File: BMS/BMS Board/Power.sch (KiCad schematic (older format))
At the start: 16 parts, among them K1 G5PZ-1A_DC12, M21 AO3402, P1 Power_Pad, P2 Power_Pad, P3 Power_Pad, P4 Power_Pad, P5 Power_Pad, P6 Power_Pad, Q1 STD12N60DM2AG

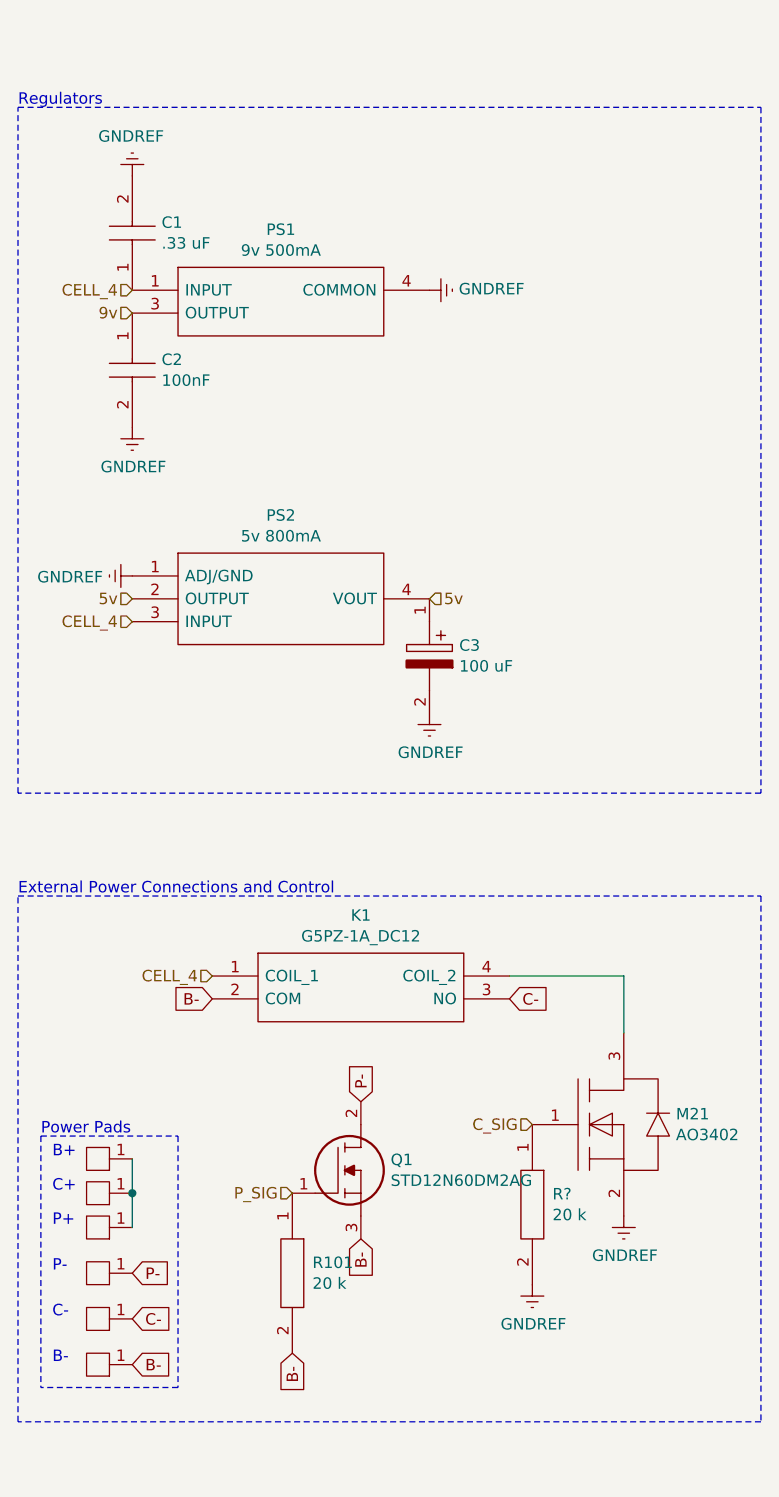
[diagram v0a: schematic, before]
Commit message: changed ui components to be classes instead of methods in Screen class
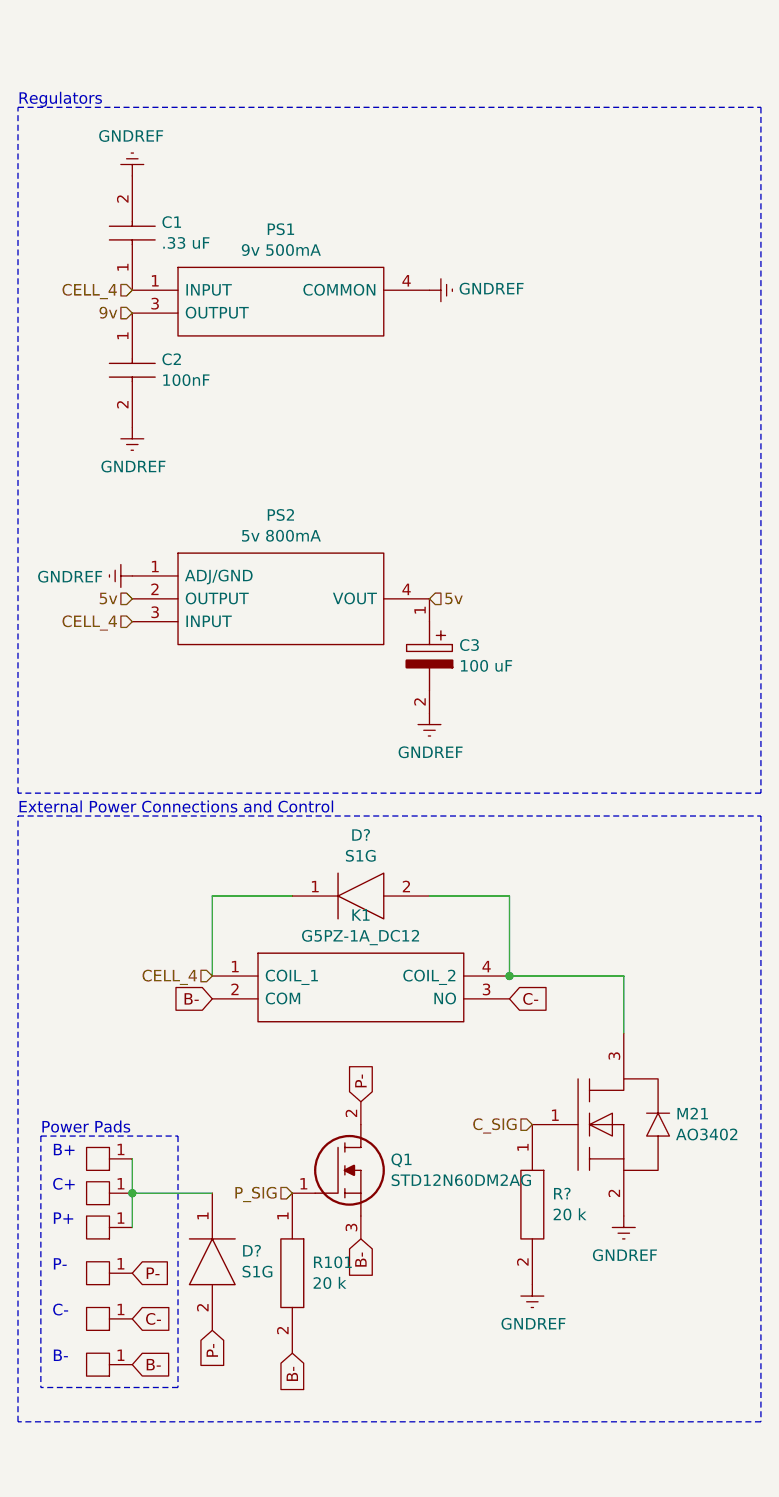
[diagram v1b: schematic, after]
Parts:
- added D? (x2): S1G, DIOM5227X250N, symbol SamacSys_Parts:S1G
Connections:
- net CELL_4: now also D?.1
- net P-: now also D?.2
- net at P1.1, P2.1, P3.1: now also D?.1
- net at K1.4 (COIL_2), M21.3 (D): now also D?.2
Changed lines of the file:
@@
 Text GLabel 3050 8350 2    50   Input ~ 0
 C-
-Wire Wire Line
-	3050 7650 3050 7800
 Connection ~ 3050 7800
 Wire Wire Line
@@
 Power Pads
 Wire Notes Line
-	2550 8800 2550 6500
-Wire Notes Line
-	2550 6500 5800 6500
-Wire Notes Line
-	5800 6500 5800 8800
+	2550 6150 5800 6150
 Wire Notes Line
 	5800 8800 2550 8800
-Text Notes 2550 6500 0    50   ~ 0
+Text Notes 2550 6150 0    50   ~ 0
 External Power Connections and Control
 Wire Notes Line
@@
 Text GLabel 3750 8500 3    50   Input ~ 0
 B-
+$Comp
+L SamacSys_Parts:S1G D?
+U 1 1 5EF4840C
+P 4050 6500
+F 0 "D?" H 4050 6765 50  0000 C CNN
+F 1 "S1G" H 4050 6674 50  0000 C CNN
+F 2 "DIOM5227X250N" H 3750 6150 50  0001 L CNN
+F 3 "https://www.onsemi.com/pub/Collateral/S1M-D.pdf" H 3750 6050 50  0001 L CNN
+F 4 "ON Semi 400V 1A, Diode, 2-Pin DO-214AC S1G" H 3750 5950 50  0001 L CNN "Description"
+F 5 "2.5" H 3750 5850 50  0001 L CNN "Height"
+F 6 "512-S1G" H 3750 5750 50  0001 L CNN "Mouser Part Number"
+F 7 "https://www.mouser.co.uk/ProductDetail/ON-Semiconductor-Fairchild/S1G?qs=RJwZ8kJo1mjiLbqXClupXw%3D%3D" H 3750 5650 50  0001 L CNN "Mouser Price/Stock"
+F 8 "ON Semiconductor" H 3750 5550 50  0001 L CNN "Manufacturer_Name"
+F 9 "S1G" H 3750 5450 50  0001 L CNN "Manufacturer_Part_Number"
+	1    4050 6500
+	1    0    0    -1
+$EndComp
+Wire Notes Line
+	2550 8800 2550 6150
+Wire Notes Line
+	5800 6150 5800 8800
+Wire Wire Line
+	3750 6500 3400 6500
+Wire Wire Line
+	3400 6500 3400 6850
+Wire Wire Line
+	4350 6500 4700 6500
+Wire Wire Line
+	4700 6500 4700 6850
+Connection ~ 4700 6850
+$Comp
+L SamacSys_Parts:S1G D?
+U 1 1 5EF4C90F
+P 3400 8100
+F 0 "D?" V 3354 8228 50  0000 L CNN
+F 1 "S1G" V 3445 8228 50  0000 L CNN
+F 2 "DIOM5227X250N" H 3100 7750 50  0001 L CNN
+F 3 "https://www.onsemi.com/pub/Collateral/S1M-D.pdf" H 3100 7650 50  0001 L CNN
+F 4 "ON Semi 400V 1A, Diode, 2-Pin DO-214AC S1G" H 3100 7550 50  0001 L CNN "Description"
+F 5 "2.5" H 3100 7450 50  0001 L CNN "Height"
+F 6 "512-S1G" H 3100 7350 50  0001 L CNN "Mouser Part Number"
+F 7 "https://www.mouser.co.uk/ProductDetail/ON-Semiconductor-Fairchild/S1G?qs=RJwZ8kJo1mjiLbqXClupXw%3D%3D" H 3100 7250 50  0001 L CNN "Mouser Price/Stock"
+F 8 "ON Semiconductor" H 3100 7150 50  0001 L CNN "Manufacturer_Name"
+F 9 "S1G" H 3100 7050 50  0001 L CNN "Manufacturer_Part_Number"
+	1    3400 8100
+	0    1    1    0
+$EndComp
+Wire Wire Line
+	3050 7650 3050 7800
+Wire Wire Line
+	3400 7800 3050 7800
+Text GLabel 3400 8400 3    50   Input ~ 0
+P-
 $EndSCHEMATC

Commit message: "SingleDigitNumberSelector" now blinks when idle.
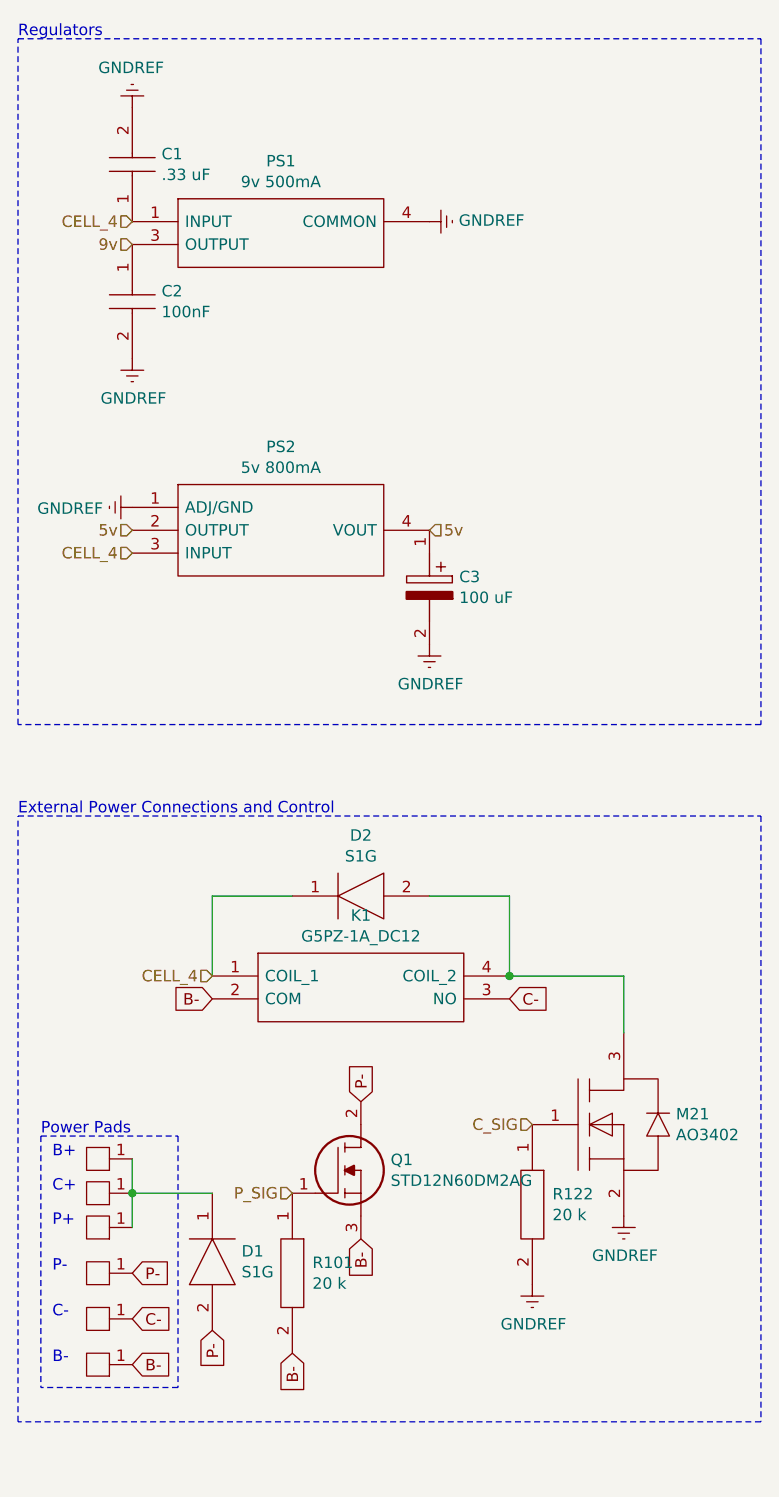
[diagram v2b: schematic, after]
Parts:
- gave numbers to parts that had none: 3
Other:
- moved on the sheet: C1, C2, C3, PS1, PS2

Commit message: ...
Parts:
- added LED3: HSMG-C170, LEDC2012X80N, symbol SamacSys_Parts:HSMG-C170
- added R143: ERJ-P06F2200V, RESC2012X70N, symbol SamacSys_Parts:ERJ-P06F2200V
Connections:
- net C_SIG: now also R143.1
- net GNDREF: now also LED3.1 (K)
- new net: LED3.2 (A), R143.2
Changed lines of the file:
@@
 P 4000 7700
 F 0 "Q1" H 4180 7746 50  0000 L CNN
-F 1 "STD12N60DM2AG" H 4180 7655 50  0000 L CNN
+F 1 "STD12N60DM2AG" H 4180 7655 50  0001 L CNN
 F 2 "STD13N60DM2" H 3750 7050 50  0001 L CNN
 F 3 "https://www.st.com/resource/en/datasheet/std12n60dm2ag.pdf" H 3750 6950 50  0001 L CNN
@@
 	-1   0    0    1
 $EndComp
-Text HLabel 4800 7500 0    50   Input ~ 0
+Text HLabel 4500 7500 0    50   Input ~ 0
 C_SIG
 Text HLabel 3750 7800 0    50   Input ~ 0
@@
 	2550 6150 5800 6150
 Wire Notes Line
-	5800 8800 2550 8800
+	5800 9050 2550 9050
 Text Notes 2550 6150 0    50   ~ 0
 External Power Connections and Control
@@
 	1    0    0    -1
 $EndComp
-Wire Notes Line
-	2550 8800 2550 6150
-Wire Notes Line
-	5800 6150 5800 8800
 Wire Wire Line
 	3750 6500 3400 6500
@@
 Text GLabel 3400 8400 3    50   Input ~ 0
 P-
+$Comp
+L SamacSys_Parts:ERJ-P06F2200V R143
+U 1 1 5EF455EC
+P 4500 7850
+F 0 "R143" V 4454 7938 50  0000 L CNN
+F 1 "ERJ-P06F2200V" H 4350 7600 50  0001 L CNN
+F 2 "RESC2012X70N" H 4350 7500 50  0001 L CNN
+F 3 "https://componentsearchengine.com/Datasheets/1/ERJ-P06F2200V.pdf" H 4700 7800 50  0001 L CNN
+F 4 "Thick Film Resistors - SMD 0805 220ohms 0.5W 1% AEC-Q200" H 4350 7400 50  0001 L CNN "Description"
+F 5 "0.7" H 4350 7300 50  0001 L CNN "Height"
+F 6 "667-ERJ-P06F2200V" H 4350 7200 50  0001 L CNN "Mouser Part Number"
+F 7 "https://www.mouser.com/Search/Refine.aspx?Keyword=667-ERJ-P06F2200V" H 4350 7100 50  0001 L CNN "Mouser Price/Stock"
+F 8 "Panasonic" H 4350 7000 50  0001 L CNN "Manufacturer_Name"
+F 9 "ERJ-P06F2200V" H 4350 6900 50  0001 L CNN "Manufacturer_Part_Number"
+F 10 "220" V 4545 7938 50  0000 L CNN "Resistance"
+	1    4500 7850
+	0    1    1    0
+$EndComp
+$Comp
+L SamacSys_Parts:HSMG-C170 LED3
+U 1 1 5EF477B4
+P 4500 8450
+F 0 "LED3" V 4496 8322 50  0000 R CNN
+F 1 "HSMG-C170" V 4405 8322 50  0000 R CNN
+F 2 "LEDC2012X80N" H 4250 8050 50  0001 L BNN
+F 3 "" H 4650 8500 50  0001 L BNN
+F 4 "Green LED, 15 mcd 170 , 2-pin 0805 SMD Package" H 4250 7950 50  0001 L BNN "Description"
+F 5 "0.8" H 4250 7850 50  0001 L BNN "Height"
+F 6 "630-HSMG-C170" H 4250 7750 50  0001 L BNN "Mouser Part Number"
+F 7 "https://www.mouser.co.uk/ProductDetail/Broadcom-Avago/HSMG-C170?qs=YDL0qNrpDT4lm8ArMPkMEA%3D%3D" H 4250 7650 50  0001 L BNN "Mouser Price/Stock"
+F 8 "Avago Technologies" H 4250 7550 50  0001 L BNN "Manufacturer_Name"
+F 9 "HSMG-C170" H 4250 7450 50  0001 L BNN "Manufacturer_Part_Number"
+	1    4500 8450
+	0    -1   -1   0
+$EndComp
+$Comp
+L power:GNDREF #PWR0155
+U 1 1 5EF48294
+P 4500 8800
+F 0 "#PWR0155" H 4500 8550 50  0001 C CNN
+F 1 "GNDREF" H 4505 8627 50  0000 C CNN
+F 2 "" H 4500 8800 50  0001 C CNN
+F 3 "" H 4500 8800 50  0001 C CNN
+	1    4500 8800
+	1    0    0    -1
+$EndComp
+Wire Notes Line
+	2550 9050 2550 6150
+Wire Notes Line
+	5800 6150 5800 9050
+Wire Wire Line
+	4500 7500 4800 7500
+Connection ~ 4800 7500
 $EndSCHEMATC

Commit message: workin on BMS also reset my computer so KiCad added some recovery files
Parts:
- M21: symbol MOSFET:AO3402 -> BMS-Board-rescue:AO3402-MOSFET
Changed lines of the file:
@@
 CELL_4
 $Comp
-L MOSFET:AO3402 M21
+L BMS-Board-rescue:AO3402-MOSFET M21
 U 1 1 5F4C2875
 P 5200 7500
+AR Path="/5F4C2875" Ref="M21"  Part="1"
+AR Path="/5E9A2B9F/5F4C2875" Ref="M21"  Part="1"
 F 0 "M21" H 5428 7546 50  0000 L CNN
 F 1 "AO3402" H 5428 7455 50  0000 L CNN
